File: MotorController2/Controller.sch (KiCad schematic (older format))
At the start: 24 parts

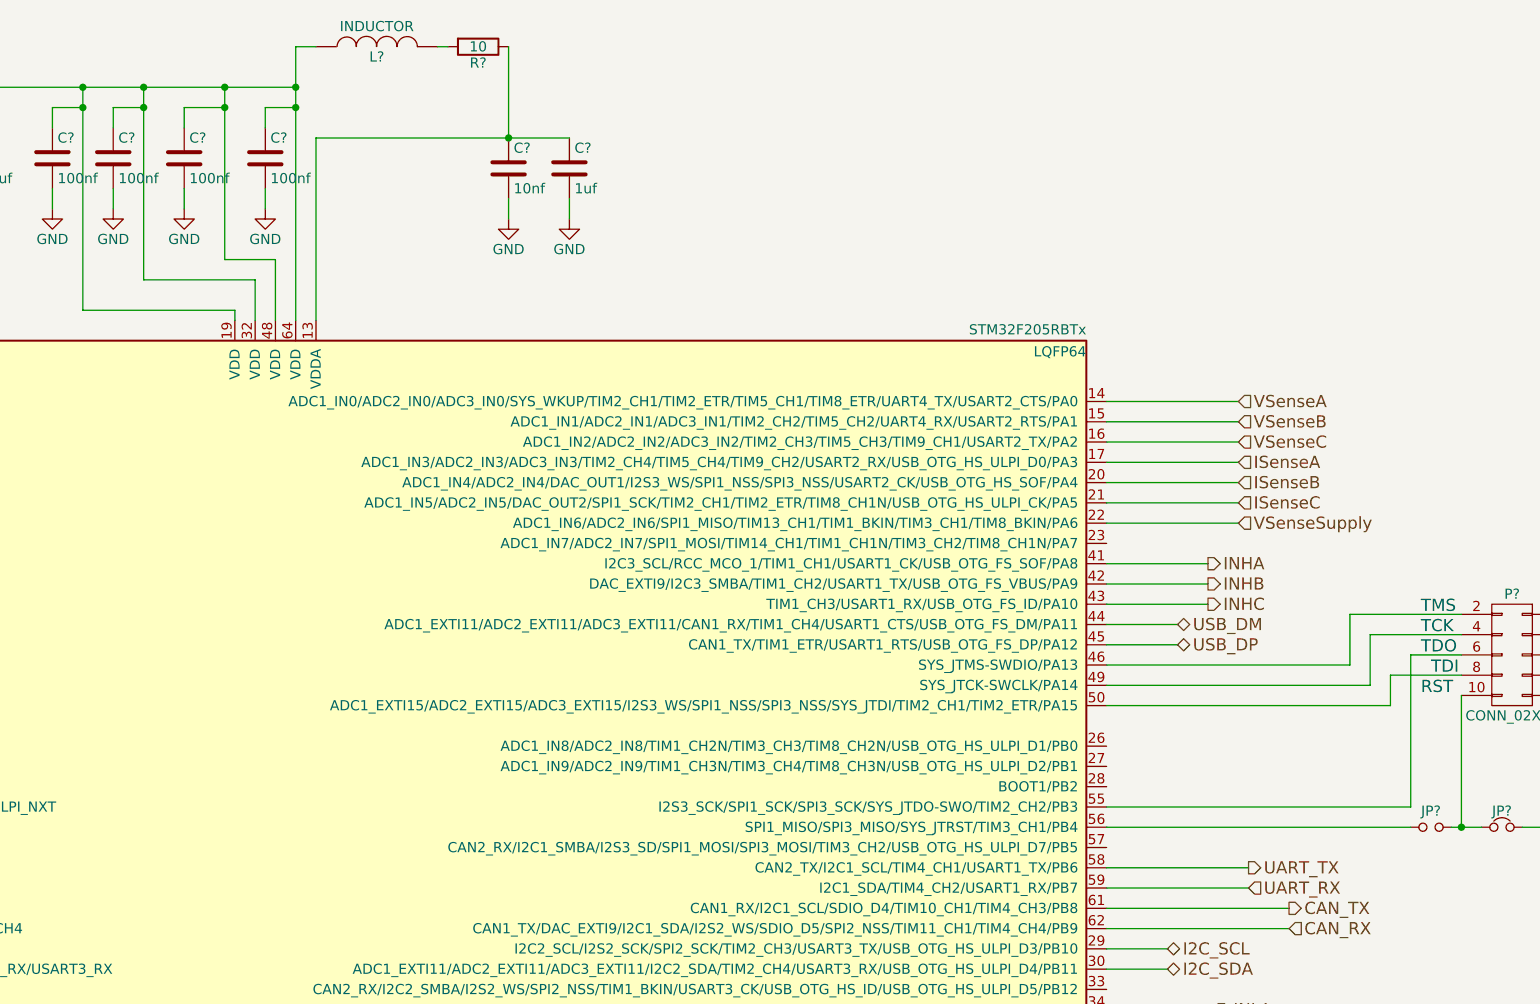
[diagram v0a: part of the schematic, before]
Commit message: Most of new motor controller schematic, and leg V2.
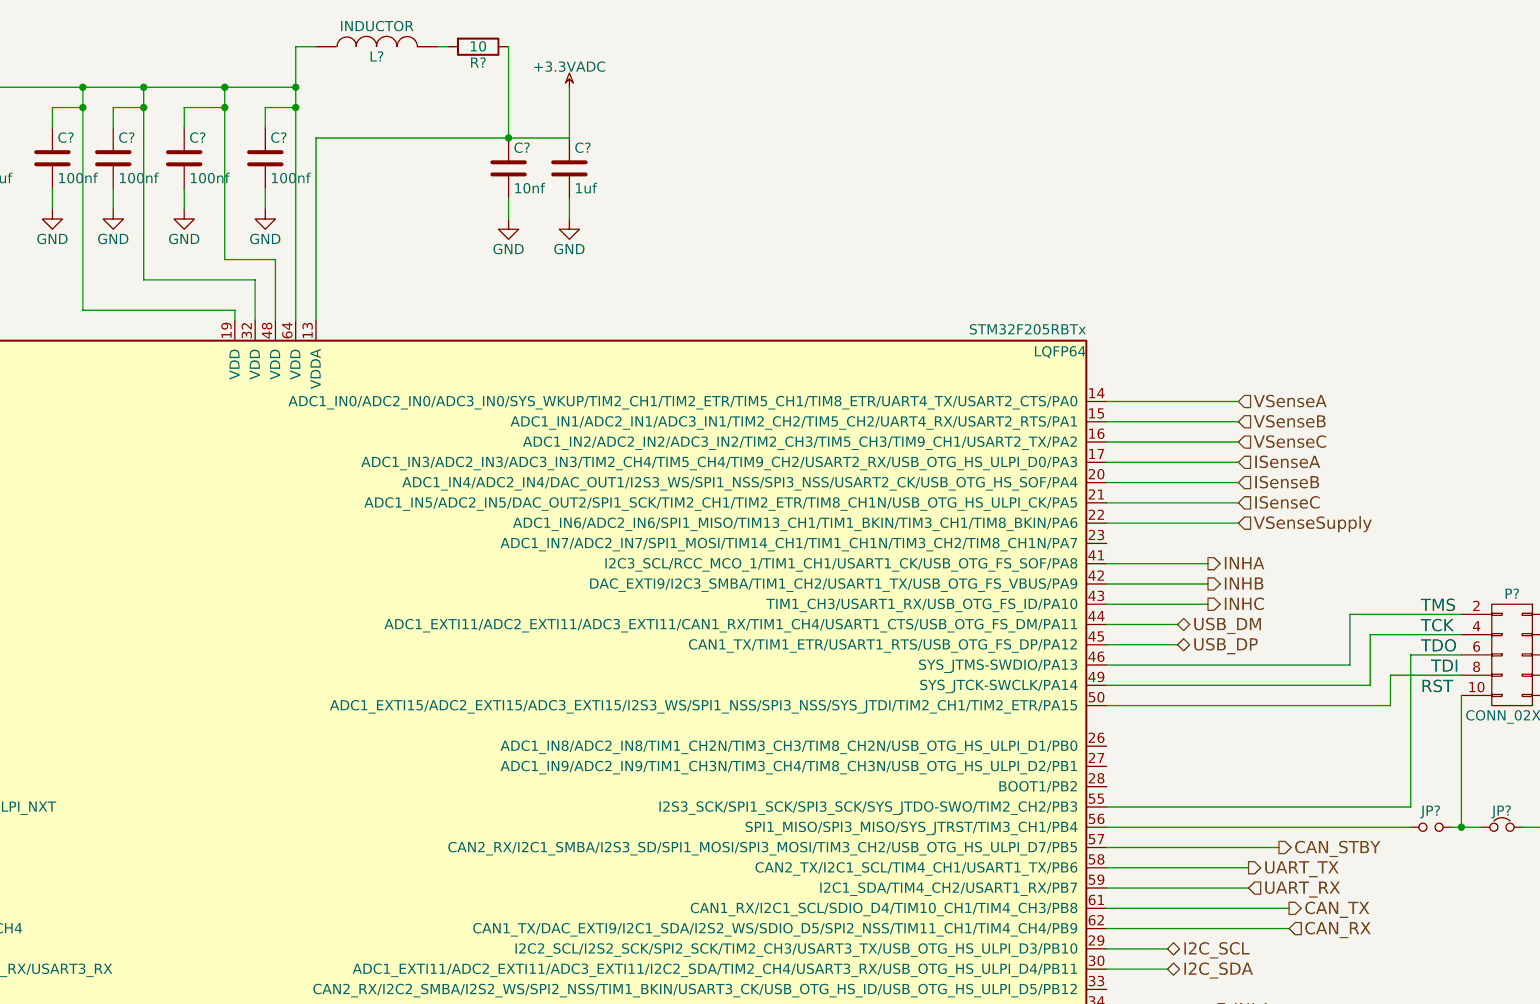
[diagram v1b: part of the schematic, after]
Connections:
- net labels added: +3.3VADC, CAN_STBY
- wire segments 134 -> 136
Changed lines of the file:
@@
 LIBS:drv8305
 LIBS:bsc016n06ns
+LIBS:dc-dc
+LIBS:IFX91041EJV33
 LIBS:BMC2-cache
 EELAYER 25 0
@@
 $Descr A3 16535 11693
 encoding utf-8
-Sheet 2 3
+Sheet 2 4
 Title ""
 Date ""
@@
 	8700 3850 8700 3550
 Wire Wire Line
-	8700 3550 8450 3550
-Wire Wire Line
-	8450 3550 8450 2700
+	8450 3550 8700 3550
+Wire Wire Line
+	8450 2700 8450 3550
 Wire Wire Line
 	8450 2800 8250 2800
@@
 	8600 3850 8600 3650
 Wire Wire Line
-	8600 3650 8050 3650
-Wire Wire Line
-	8050 3650 8050 2700
+	8050 3650 8600 3650
+Wire Wire Line
+	8050 2700 8050 3650
 Wire Wire Line
 	8050 2800 7900 2800
@@
 Wire Wire Line
 	4300 5750 4600 5750
+$Comp
+L +3.3VADC #PWR?
+U 1 1 585F9182
+P 10150 2700
+F 0 "#PWR?" H 10300 2650 50  0001 C CNN
+F 1 "+3.3VADC" H 10150 2800 50  0000 C CNN
+F 2 "" H 10150 2700 50  0000 C CNN
+F 3 "" H 10150 2700 50  0000 C CNN
+	1    10150 2700
+	1    0    0    -1
+$EndComp
+Wire Wire Line
+	10150 2950 10150 2700
+Text HLabel 13650 6450 2    60   Output ~ 0
+CAN_STBY
+Wire Wire Line
+	13650 6450 12800 6450
 $EndSCHEMATC

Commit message: Initial schematic complete.
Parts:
- added C? (x2): 0.1uF 5V, symbol C
- added R? (x4): 10K, symbol R
- added SW?: CAL, symbol SW_PUSH
- C? (x2): value C -> 15pF
- C?: value 100nf -> 100nf 5V
- SW?: value SW_PUSH -> RESET
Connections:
- net labels added: +5V, TempDrv
- wire segments 136 -> 159
- no-connect marks 1 -> 2

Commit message: Component footprints.
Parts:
- removed X?: 8MHz, symbol CRYSTAL_SMD
- added W14: PB12, Measurement_Points:Measurement_Point_Round-SMD-Pad_Big, symbol TEST_1P
- added X1: 8MHz, Crystals:Crystal_HC49-SD_SMD, symbol Crystal
- C10, C11, C12, C13, C14, C15, C16, C3, C4, C5, C6, C7, C9: renamed from C?; footprint (none) -> Capacitors_SMD:C_0805_HandSoldering
- C8: renamed from C?; footprint (none) -> Capacitors_SMD:C_1206_HandSoldering
- D2, D3: renamed from D?; footprint (none) -> LEDs:LED_0805
- JP1, JP2: renamed from JP?; footprint (none) -> Resistors_SMD:R_0805_HandSoldering
- L1: renamed from L?; value INDUCTOR -> 10uH; footprint (none) -> Resistors_SMD:R_0805_HandSoldering
- R11, R12, R13, R14, R15, R16, R17: renamed from R?; footprint (none) -> Resistors_SMD:R_0805_HandSoldering
- SW1: renamed from SW?; footprint (none) -> Buttons_Switches_SMD:SW_SPST_FSMSM
- SW2: renamed from SW?; footprint (none) -> Buttons_Switches_SMD:SW_SPST_FSMSM; Order (none) -> http://uk.farnell.com/alcoswitch-te-connectivity/1437566-3/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
- U2: renamed from U?; footprint LQFP64 -> Housings_QFP:LQFP-64_10x10mm_Pitch0.5mm
- gave numbers to parts that had none: 1
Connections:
- wire segments 159 -> 163

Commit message: Add local library.
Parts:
- P8: footprint (none) -> Local:SMT-HDR-10; Order (none) -> http://uk.rs-online.com/web/p/pcb-headers/0451732/?searchTe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
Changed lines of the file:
@@
 $EndComp
 $Comp
-L GND #PWR018
+L GND #PWR020
 U 1 1 5856B3FF
 P 3350 5650
-F 0 "#PWR018" H 3350 5400 50  0001 C CNN
+F 0 "#PWR020" H 3350 5400 50  0001 C CNN
 F 1 "GND" H 3350 5500 50  0000 C CNN
 F 2 "" H 3350 5650 50  0000 C CNN
@@
 F 0 "P8" H 14800 5800 50  0000 C CNN
 F 1 "CONN_02X05" H 14800 5200 50  0000 C CNN
-F 2 "" H 14800 4300 50  0001 C CNN
+F 2 "Local:SMT-HDR-10" H 14800 4300 50  0001 C CNN
 F 3 "" H 14800 4300 50  0000 C CNN
+F 4 "http://uk.rs-online.com/web/p/pcb-headers/0451732/?searchTerm=FTSH-105-01-F-DV-K&autocorrected=y&relevancy-data=636F3D3526696E3D4931384E4D616E506172744E756D626572266C753D656E266D6D3D6D61746368616C6C7061727469616C26706D3D5E5B5C707B4C7D5C707B4E647D2D2C2F255C2E5D2B2426706F3D3226736E3D592673723D4175746F636F727265637465642673613D6674736831303530316664762673743D4B4559574F52445F53494E474C455F414C5048415F4E554D455249432673633D592677633D4E4F4E45267573743D465453482D3130352D30312D462D44562D4B267374613D4654534831303530314644564B26" H 14800 5500 60  0001 C CNN "Order"
 	1    14800 5500
 	-1   0    0    -1
 $EndComp
 $Comp
-L +3V3 #PWR019
+L +3V3 #PWR021
 U 1 1 585859AF
 P 15250 5150
-F 0 "#PWR019" H 15250 5000 50  0001 C CNN
+F 0 "#PWR021" H 15250 5000 50  0001 C CNN
 F 1 "+3V3" H 15250 5290 50  0000 C CNN
 F 2 "" H 15250 5150 50  0000 C CNN
@@
 $EndComp
 $Comp
-L GND #PWR020
+L GND #PWR022
 U 1 1 585859E1
 P 15300 5850
-F 0 "#PWR020" H 15300 5600 50  0001 C CNN
+F 0 "#PWR022" H 15300 5600 50  0001 C CNN
 F 1 "GND" H 15300 5700 50  0000 C CNN
 F 2 "" H 15300 5850 50  0000 C CNN
@@
 $EndComp
 $Comp
-L GND #PWR021
+L GND #PWR023
 U 1 1 585D756A
 P 8650 3300
-F 0 "#PWR021" H 8650 3050 50  0001 C CNN
+F 0 "#PWR023" H 8650 3050 50  0001 C CNN
 F 1 "GND" H 8650 3150 50  0000 C CNN
 F 2 "" H 8650 3300 50  0000 C CNN
@@
 $EndComp
 $Comp
-L GND #PWR022
+L GND #PWR024
 U 1 1 585D75A0
 P 8250 3300
-F 0 "#PWR022" H 8250 3050 50  0001 C CNN
+F 0 "#PWR024" H 8250 3050 50  0001 C CNN
 F 1 "GND" H 8250 3150 50  0000 C CNN
 F 2 "" H 8250 3300 50  0000 C CNN
@@
 $EndComp
 $Comp
-L GND #PWR023
+L GND #PWR025
 U 1 1 585D75CF
 P 7900 3300
-F 0 "#PWR023" H 7900 3050 50  0001 C CNN
+F 0 "#PWR025" H 7900 3050 50  0001 C CNN
 F 1 "GND" H 7900 3150 50  0000 C CNN
 F 2 "" H 7900 3300 50  0000 C CNN
@@
 $EndComp
 $Comp
-L GND #PWR024
+L GND #PWR026
 U 1 1 585D75FE
 P 7600 3300
-F 0 "#PWR024" H 7600 3050 50  0001 C CNN
+F 0 "#PWR026" H 7600 3050 50  0001 C CNN
 F 1 "GND" H 7600 3150 50  0000 C CNN
 F 2 "" H 7600 3300 50  0000 C CNN
@@
 $EndComp
 $Comp
-L GND #PWR025
+L GND #PWR027
 U 1 1 585D7A19
 P 7200 3300
-F 0 "#PWR025" H 7200 3050 50  0001 C CNN
+F 0 "#PWR027" H 7200 3050 50  0001 C CNN
 F 1 "GND" H 7200 3150 50  0000 C CNN
 F 2 "" H 7200 3300 50  0000 C CNN
@@
 $EndComp
 $Comp
-L +3V3 #PWR026
+L +3V3 #PWR028
 U 1 1 585D7AA9
 P 7200 2600
-F 0 "#PWR026" H 7200 2450 50  0001 C CNN
+F 0 "#PWR028" H 7200 2450 50  0001 C CNN
 F 1 "+3V3" H 7200 2740 50  0000 C CNN
 F 2 "" H 7200 2600 50  0000 C CNN
@@
 $EndComp
 $Comp
-L GND #PWR027
+L GND #PWR029
 U 1 1 585D7D30
 P 9850 3350
-F 0 "#PWR027" H 9850 3100 50  0001 C CNN
+F 0 "#PWR029" H 9850 3100 50  0001 C CNN
 F 1 "GND" H 9850 3200 50  0000 C CNN
 F 2 "" H 9850 3350 50  0000 C CNN
@@
 $EndComp
 $Comp
-L GND #PWR028
+L GND #PWR030
 U 1 1 585D7D5F
 P 10150 3350
-F 0 "#PWR028" H 10150 3100 50  0001 C CNN
+F 0 "#PWR030" H 10150 3100 50  0001 C CNN
 F 1 "GND" H 10150 3200 50  0000 C CNN
 F 2 "" H 10150 3350 50  0000 C CNN
@@
 $EndComp
 $Comp
-L GND #PWR029
+L GND #PWR031
 U 1 1 585D84A2
 P 4000 4000
-F 0 "#PWR029" H 4000 3750 50  0001 C CNN
+F 0 "#PWR031" H 4000 3750 50  0001 C CNN
 F 1 "GND" H 4000 3850 50  0000 C CNN
 F 2 "" H 4000 4000 50  0000 C CNN
@@
 $EndComp
 $Comp
-L GND #PWR030
+L GND #PWR032
 U 1 1 585D874F
 P 3300 3750
-F 0 "#PWR030" H 3300 3500 50  0001 C CNN
+F 0 "#PWR032" H 3300 3500 50  0001 C CNN
 F 1 "GND" H 3300 3600 50  0000 C CNN
 F 2 "" H 3300 3750 50  0000 C CNN
@@
 $EndComp
 $Comp
-L GND #PWR031
+L GND #PWR033
 U 1 1 585D8F48
 P 2850 5200
-F 0 "#PWR031" H 2850 4950 50  0001 C CNN
+F 0 "#PWR033" H 2850 4950 50  0001 C CNN
 F 1 "GND" H 2850 5050 50  0000 C CNN
 F 2 "" H 2850 5200 50  0000 C CNN
@@
 Index
 $Comp
-L +3V3 #PWR032
+L +3V3 #PWR034
 U 1 1 585DAE20
 P 4200 4600
-F 0 "#PWR032" H 4200 4450 50  0001 C CNN
+F 0 "#PWR034" H 4200 4450 50  0001 C CNN
 F 1 "+3V3" H 4200 4740 50  0000 C CNN
 F 2 "" H 4200 4600 50  0000 C CNN
@@
 $EndComp
 $Comp
-L GND #PWR033
+L GND #PWR035
 U 1 1 585DBFC1
 P 8800 8050
-F 0 "#PWR033" H 8800 7800 50  0001 C CNN
+F 0 "#PWR035" H 8800 7800 50  0001 C CNN
 F 1 "GND" H 8800 7900 50  0000 C CNN
 F 2 "" H 8800 8050 50  0000 C CNN
@@
 	12800 4750 13450 4750
 $Comp
-L GND #PWR034
+L GND #PWR036
 U 1 1 585DF79E
 P 4300 4250
-F 0 "#PWR034" H 4300 4000 50  0001 C CNN
+F 0 "#PWR036" H 4300 4000 50  0001 C CNN
 F 1 "GND" H 4300 4100 50  0000 C CNN
 F 2 "" H 4300 4250 50  0000 C CNN
@@
 $EndComp
 $Comp
-L GND #PWR035
+L GND #PWR037
 U 1 1 585E0B52
 P 3000 7300
-F 0 "#PWR035" H 3000 7050 50  0001 C CNN
+F 0 "#PWR037" H 3000 7050 50  0001 C CNN
 F 1 "GND" H 3000 7150 50  0000 C CNN
 F 2 "" H 3000 7300 50  0000 C CNN
@@
 $EndComp
 $Comp
-L GND #PWR036
+L GND #PWR038
 U 1 1 585E0CBA
 P 3250 7300
-F 0 "#PWR036" H 3250 7050 50  0001 C CNN
+F 0 "#PWR038" H 3250 7050 50  0001 C CNN
 F 1 "GND" H 3250 7150 50  0000 C CNN
 F 2 "" H 3250 7300 50  0000 C CNN
@@
 $EndComp
 $Comp
-L GND #PWR037
+L GND #PWR039
 U 1 1 586D9B9E
 P 14750 7500
-F 0 "#PWR037" H 14750 7250 50  0001 C CNN
+F 0 "#PWR039" H 14750 7250 50  0001 C CNN
 F 1 "GND" H 14750 7350 50  0000 C CNN
 F 2 "" H 14750 7500 50  0000 C CNN
@@
 $EndComp
 $Comp
-L +5V #PWR038
+L +5V #PWR040
 U 1 1 586D9C47
 P 14750 6650
-F 0 "#PWR038" H 14750 6500 50  0001 C CNN
+F 0 "#PWR040" H 14750 6500 50  0001 C CNN
 F 1 "+5V" H 14750 6790 50  0000 C CNN
 F 2 "" H 14750 6650 50  0000 C CNN
@@
 Connection ~ 14250 6350
 $Comp
-L +3V3 #PWR039
+L +3V3 #PWR041
 U 1 1 586FC541
 P 14500 6950
-F 0 "#PWR039" H 14500 6800 50  0001 C CNN
+F 0 "#PWR041" H 14500 6800 50  0001 C CNN
 F 1 "+3V3" H 14500 7090 50  0000 C CNN
 F 2 "" H 14500 6950 50  0000 C CNN
@@
 $EndComp
 $Comp
-L +3V3 #PWR040
+L +3V3 #PWR042
 U 1 1 586FE559
 P 14100 7250
-F 0 "#PWR040" H 14100 7100 50  0001 C CNN
+F 0 "#PWR042" H 14100 7100 50  0001 C CNN
 F 1 "+3V3" H 14100 7390 50  0000 C CNN
 F 2 "" H 14100 7250 50  0000 C CNN
@@
 	14100 7650 14100 7750
 $Comp
-L GND #PWR041
+L GND #PWR043
 U 1 1 586FE773
 P 14100 8450
-F 0 "#PWR041" H 14100 8200 50  0001 C CNN
+F 0 "#PWR043" H 14100 8200 50  0001 C CNN
 F 1 "GND" H 14100 8300 50  0000 C CNN
 F 2 "" H 14100 8450 50  0000 C CNN
@@
 	12800 7150 13650 7150
 $Comp
-L +3.3VADC #PWR042
+L +3.3VADC #PWR044
 U 1 1 585F9182
 P 10150 2700
-F 0 "#PWR042" H 10300 2650 50  0001 C CNN
+F 0 "#PWR044" H 10300 2650 50  0001 C CNN
 F 1 "+3.3VADC" H 10150 2800 50  0000 C CNN
 F 2 "" H 10150 2700 50  0000 C CNN
@@
 $EndComp
 $Comp
-L PWR_FLAG #FLG043
+L PWR_FLAG #FLG045
 U 1 1 587638B7
 P 10500 2800
-F 0 "#FLG043" H 10500 2895 50  0001 C CNN
+F 0 "#FLG045" H 10500 2895 50  0001 C CNN
 F 1 "PWR_FLAG" H 10500 2980 50  0000 C CNN
 F 2 "" H 10500 2800 50  0000 C CNN
@@
 NoConn ~ 12800 4950
 $Comp
-L PWR_FLAG #FLG044
+L PWR_FLAG #FLG046
 U 1 1 587659B8
 P 3300 4500
-F 0 "#FLG044" H 3300 4595 50  0001 C CNN
+F 0 "#FLG046" H 3300 4595 50  0001 C CNN
 F 1 "PWR_FLAG" H 3300 4680 50  0000 C CNN
 F 2 "" H 3300 4500 50  0000 C CNN
@@
 $EndComp
 $Comp
-L PWR_FLAG #FLG045
+L PWR_FLAG #FLG047
 U 1 1 58765F43
 P 3600 4550
-F 0 "#FLG045" H 3600 4645 50  0001 C CNN
+F 0 "#FLG047" H 3600 4645 50  0001 C CNN
 F 1 "PWR_FLAG" H 3600 4730 50  0000 C CNN
 F 2 "" H 3600 4550 50  0000 C CNN

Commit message: Laying out power section.
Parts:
- D2, D3: symbol LED -> LED-RESCUE-BMC2
- W14: footprint Measurement_Points:Measurement_Point_Round-SMD-Pad_Big -> Measurement_Points:Measurement_Point_Round-SMD-Pad_Small
- X1: footprint Crystals:Crystal_HC49-SD_SMD -> Crystals:ABM3; Order http://uk.farnell.com/qantek-technology-corporation/qcs8-00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 -> http://uk.farnell.com/abracon/abm3-8-000mhz-d2y-t/crystal-8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
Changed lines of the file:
@@
 EESchema Schematic File Version 2
+LIBS:BMC2-rescue
 LIBS:power
 LIBS:device
@@
 LIBS:IFX91041EJV33
 LIBS:BMC2-cache
-EELAYER 25 0
+EELAYER 26 0
 EELAYER END
 $Descr A3 16535 11693
@@
 $EndComp
 $Comp
-L LED D2
+L LED-RESCUE-BMC2 D2
 U 1 1 585E07CB
 P 3000 7050
@@
 $EndComp
 $Comp
-L LED D3
+L LED-RESCUE-BMC2 D3
 U 1 1 585E0AF9
 P 3250 7050
@@
 F 0 "W14" H 13650 7420 50  0000 C CNN
 F 1 "PB12" H 13650 7350 50  0000 C CNN
-F 2 "Measurement_Points:Measurement_Point_Round-SMD-Pad_Big" H 13850 7150 50  0001 C CNN
+F 2 "Measurement_Points:Measurement_Point_Round-SMD-Pad_Small" H 13850 7150 50  0001 C CNN
 F 3 "" H 13850 7150 50  0000 C CNN
 	1    13650 7150
@@
 F 0 "X1" H 4000 5450 50  0000 C CNN
 F 1 "8MHz" H 4000 5150 50  0000 C CNN
-F 2 "Crystals:Crystal_HC49-SD_SMD" H 4000 5300 50  0001 C CNN
-F 3 "http://www.farnell.com/datasheets/1998804.pdf?_ga=1.267373838.1808009743.1471515981" H 4000 5300 50  0001 C CNN
-F 4 "http://uk.farnell.com/qantek-technology-corporation/qcs8-00000f18b23m/crystal-8mhz-18pf-12-5mm-x-4-6mm/dp/2508478" H 4000 5300 60  0001 C CNN "Order"
+F 2 "Crystals:ABM3" H 4000 5300 50  0001 C CNN
+F 3 "http://www.farnell.com/datasheets/1754353.pdf?_ga=1.70757648.1808009743.1471515981" H 4000 5300 50  0001 C CNN
+F 4 "http://uk.farnell.com/abracon/abm3-8-000mhz-d2y-t/crystal-8mhz-18pf-smd/dp/2101329" H 4000 5300 60  0001 C CNN "Order"
 	1    4000 5300
 	0    1    1    0

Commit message: More of the layout done.
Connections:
- net INHA: now also U2.43 (TIM1_CH3/USART1_RX/USB_OTG_FS_ID/PA10); no longer U2.41 (I2C3_SCL/RCC_MCO_1/TIM1_CH1/USART1_CK/USB_OTG_FS_SOF/PA8)
- net INHC: now also U2.41 (I2C3_SCL/RCC_MCO_1/TIM1_CH1/USART1_CK/USB_OTG_FS_SOF/PA8); no longer U2.43 (TIM1_CH3/USART1_RX/USB_OTG_FS_ID/PA10)
- net INLA: now also U2.36 (ADC1_EXTI15/ADC2_EXTI15/ADC3_EXTI15/I2S2_SD/RTC_REFIN/SPI2_MOSI/TIM12_CH2/TIM1_CH3N/TIM8_CH3N/USB_OTG_HS_DP/PB15); no longer U2.34 (CAN2_TX/I2S2_SCK/SPI2_SCK/TIM1_CH1N/USART3_CTS/USB_OTG_HS_ULPI_D6/USB_OTG_HS_VBUS/PB13)
- net INLC: now also U2.34 (CAN2_TX/I2S2_SCK/SPI2_SCK/TIM1_CH1N/USART3_CTS/USB_OTG_HS_ULPI_D6/USB_OTG_HS_VBUS/PB13); no longer U2.36 (ADC1_EXTI15/ADC2_EXTI15/ADC3_EXTI15/I2S2_SD/RTC_REFIN/SPI2_MOSI/TIM12_CH2/TIM1_CH3N/TIM8_CH3N/USB_OTG_HS_DP/PB15)
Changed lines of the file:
@@
 Text HLabel 13100 6850 2    60   Input ~ 0
 CAN_RX
-Text HLabel 13300 5050 2    60   Output ~ 0
+Text HLabel 13250 5250 2    60   Output ~ 0
 INHA
-Text HLabel 13300 5150 2    60   Output ~ 0
+Text HLabel 13250 5150 2    60   Output ~ 0
 INHB
-Text HLabel 13300 5250 2    60   Output ~ 0
+Text HLabel 13250 5050 2    60   Output ~ 0
 INHC
-Text HLabel 13100 7250 2    60   Output ~ 0
+Text HLabel 13100 7450 2    60   Output ~ 0
 INLA
 Text HLabel 13100 7350 2    60   Output ~ 0
 INLB
-Text HLabel 13100 7450 2    60   Output ~ 0
+Text HLabel 13100 7250 2    60   Output ~ 0
 INLC
 Text HLabel 4300 7350 0    60   Output ~ 0
@@
 	4350 6050 4600 6050
 Wire Wire Line
-	12800 5050 13300 5050
-Wire Wire Line
-	12800 5150 13300 5150
-Wire Wire Line
-	12800 5250 13300 5250
-Wire Wire Line
-	12800 7250 13100 7250
-Wire Wire Line
-	12800 7350 13100 7350
-Wire Wire Line
-	12800 7450 13100 7450
-Wire Wire Line
 	4350 6150 4600 6150
 Wire Wire Line
@@
 Wire Wire Line
 	4000 5150 4000 5100
+Wire Wire Line
+	12800 5050 13250 5050
+Wire Wire Line
+	12800 5150 13250 5150
+Wire Wire Line
+	12800 5250 13250 5250
+Wire Wire Line
+	13100 7250 12800 7250
+Wire Wire Line
+	12800 7350 13100 7350
+Wire Wire Line
+	12800 7450 13100 7450
 $EndSCHEMATC

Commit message: Work on BOM.
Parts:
- C10, C11, C12, C7: value 100nf -> 0.1uF 50V
- C13: value 10nf -> 0.1uF 50V
- C14: value 1uf -> 1uF 50V; Farnell (none) -> 1759432; Notes (none) -> 5V
- C15, C16: value 0.1uF 5V -> 0.1uF 50V
- C3, C4: value 2.2uf -> 2.2uF 50V; Farnell (none) -> 2611933
- C5: Farnell (none) -> 2497014
- C8: value 4.7uf -> 4.7uF 25V; Farnell (none) -> 1828835
- C9: value 100nf 5V -> 0.1uF 50V
- D2: Farnell (none) -> 1465996; Notes (none) -> 2V
- D3: value RED LED -> YELLOW; Farnell (none) -> 1581241
- L1: Farnell (none) -> 2215650
- R13: value 10 -> 10R
- SW1: Farnell (none) -> 42468741
- SW2: Farnell (none) -> 2468741
- X1: Farnell (none) -> 2101329
